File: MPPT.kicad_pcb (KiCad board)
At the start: 2 copper layers, 172.7 x 116.8 mm, 155 parts, among them J1 Solar Array, J2 Battery, J3 Car Power, J4 CAN_In, J5 CAN_Out, Q1 NMOS, Q2 NMOS, SW1 RESET, SW2 CAN Address, U1 PQMC3-D12-S9-S, U2 Nucleo_L432KC, U3 UCC37321, U4 INA210, U5 ADM3055E, U6 INA210, U7 CDSOT23-T24CAN

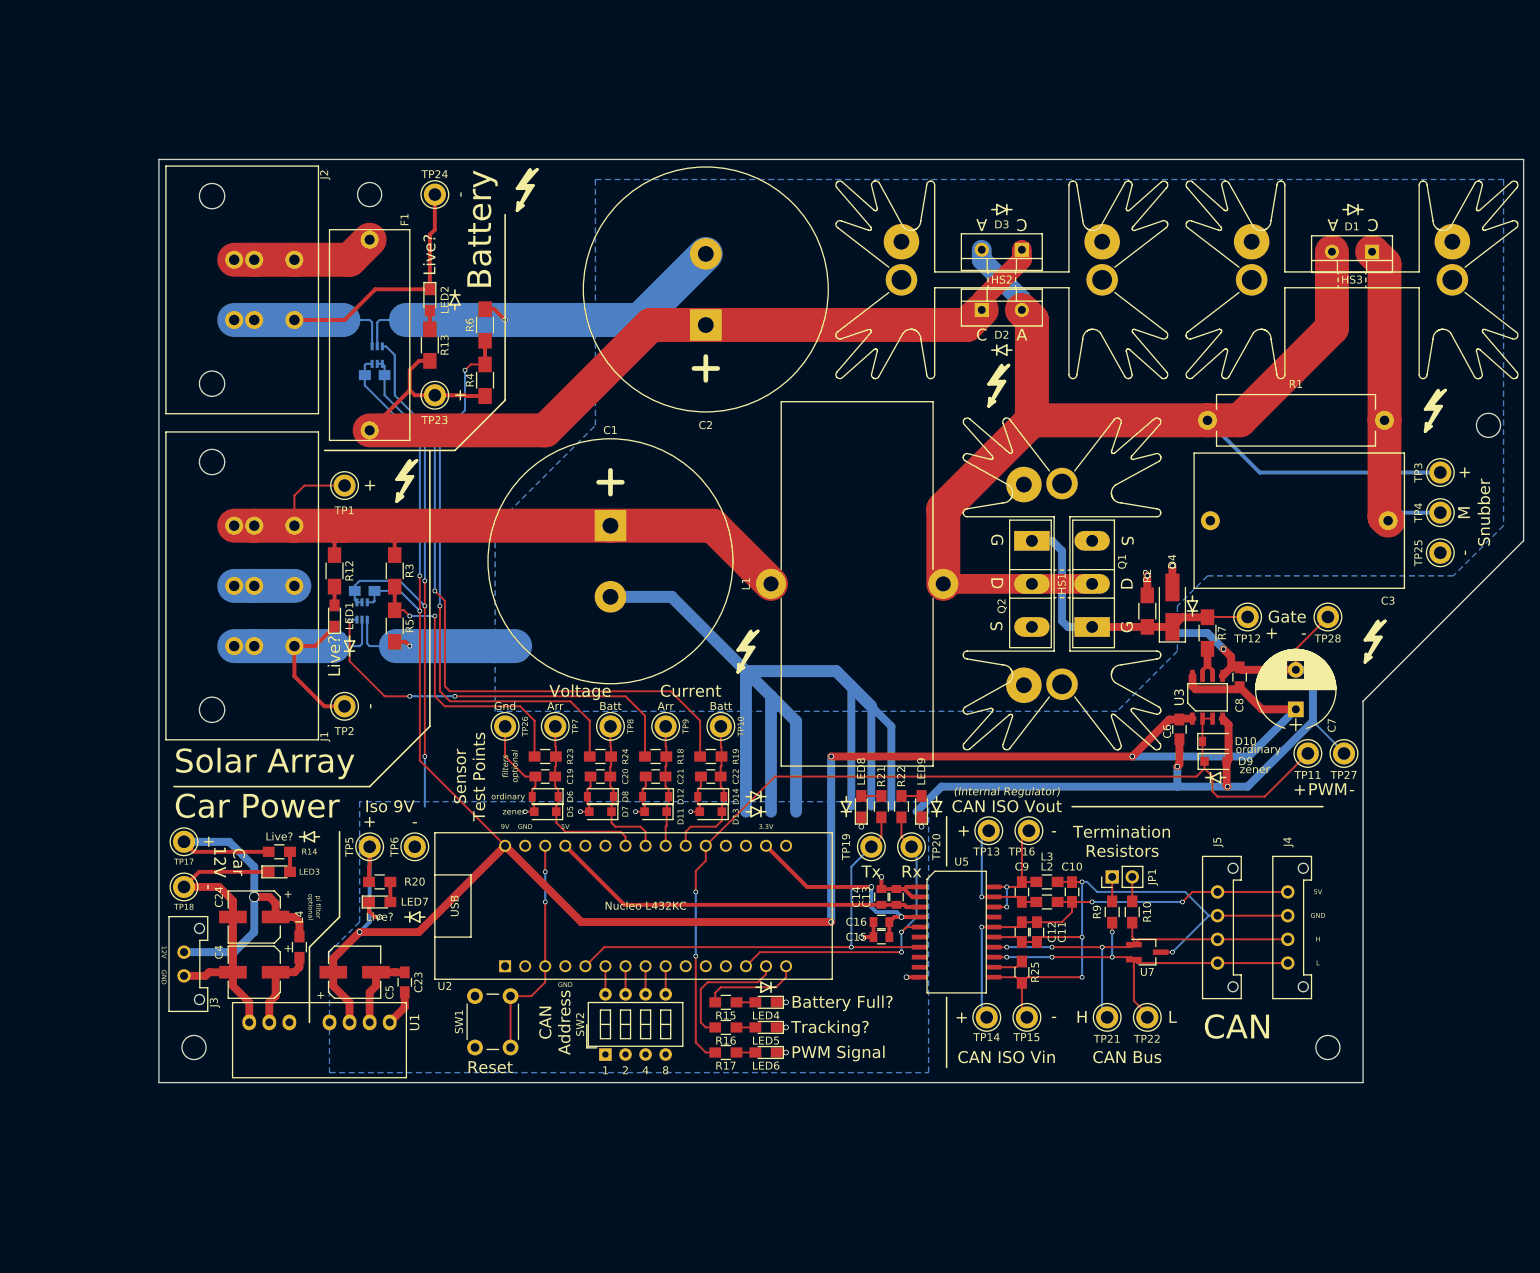
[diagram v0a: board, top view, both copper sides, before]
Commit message: Major MPPT Board overhaul. Schematic advanced to Rev 3.2. Layout advanced to Rev 1.3. README and documentation updated. Parts list synchronized, standardized, and referenced.
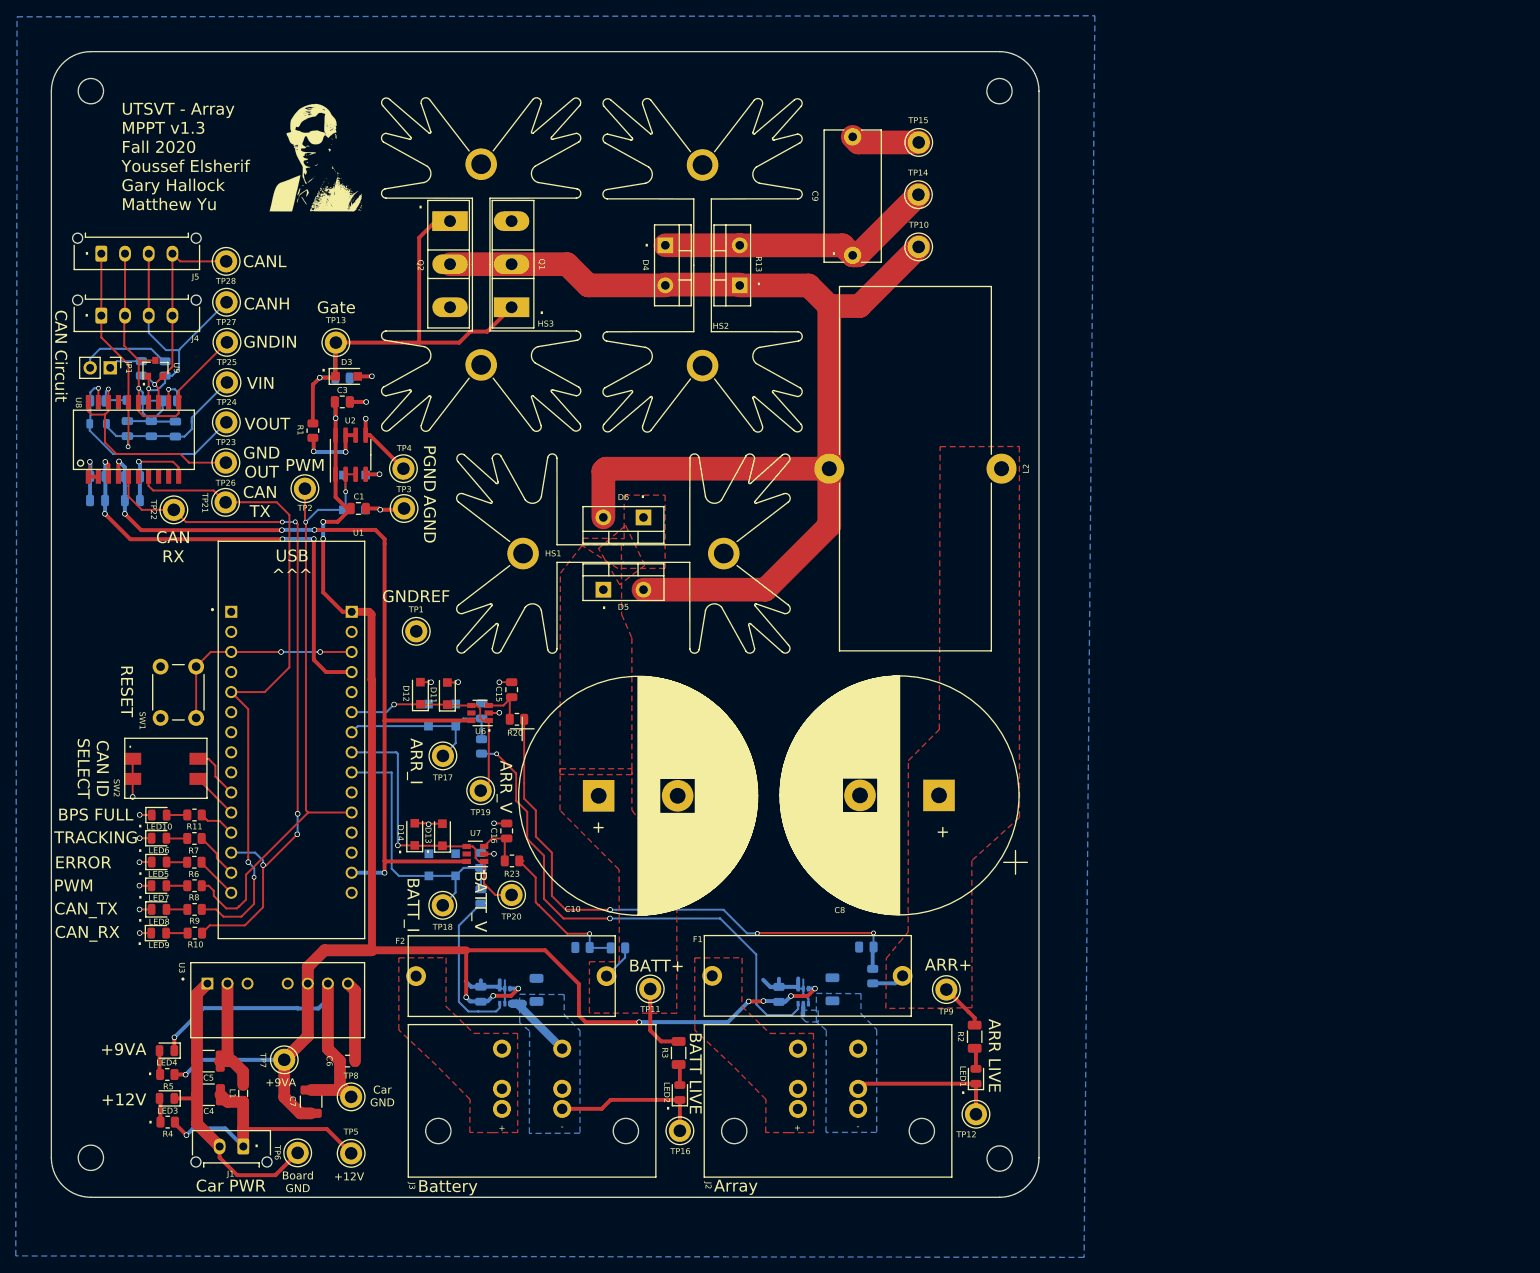
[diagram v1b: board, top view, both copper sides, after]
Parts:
- removed REF** (x6): Symbol_HighVoltage_Small, UTSVT_Special:Symbol_HighVoltage_Small
- removed REF** (x6): SolderWirePad_single_2mmDrill, Wire_Pads:SolderWirePad_single_2mmDrill
- removed REF** (x4): MountingHole_4-40_PanHead, UTSVT_Mechanical:MountingHole_4-40_PanHead
- removed REF** (x14): Diode_Symbol_Small, UTSVT_Special:Diode_Symbol_Small
- added F2: Fuse, MPPT-PrimaryPCB:05200101Z_Fuze_Holder_5x20_PCB_Mount, F.Cu at (62.7, 129.4)
- added G***: LOGO, UTSVT_Special:UTSVT_Logo_Symbol, B.Cu at (35.9, 27.7)
- added G***: LOGO, UTSVT_Special:Hallock_Image_Tiny, F.Cu at (50.5, 30.7)
- added H1: Top Left Mounting Hole, MountingHole:MountingHole_3.2mm_M3, F.Cu at (137.5, 157.5)
- added H2: Top Right Mounting Hole, MountingHole:MountingHole_3.2mm_M3, F.Cu at (22.5, 157.5)
- added H3: Bottom Left Mounting Hole, MountingHole:MountingHole_3.2mm_M3, F.Cu at (137.5, 22.5)
- added H4: Bottom Right Mounting Hole, MountingHole:MountingHole_3.2mm_M3, F.Cu at (22.5, 22.5)
- added LED10: BPS Full (Blue), LED_SMD:LED_0805_2012Metric, F.Cu at (31.1, 114.1)
- added R26: 60, Resistor_SMD:R_0805_2012Metric, B.Cu at (28.9, 57.6)
- added U8: ADM3055E, MPPT-PrimaryPCB:ADM3055EBRIZ, F.Cu at (27.9, 66.5)
- added U9: CDSOT23-T24CAN, Package_TO_SOT_SMD:SOT-23, F.Cu at (30.7, 57.5)
- C1: value 1000uF -> 0.1uF; footprint UTSVT_Passive:CP_Radial_D31mm_P9mm -> Capacitor_SMD:C_0805_2012Metric
- C10: value 0.22u -> 1000uF; footprint Capacitors_SMD:C_0805_HandSoldering -> Capacitor_THT:CP_Radial_D30.0mm_P10.00mm_SnapIn
- C11: value 0.1u -> 0.1uF; footprint Capacitors_SMD:C_0805_HandSoldering -> Capacitor_SMD:C_0805_2012Metric; moved to B.Cu
- C12: value 0.01u -> 1uF; footprint Capacitors_SMD:C_0805_HandSoldering -> Capacitor_SMD:C_0805_2012Metric; moved to B.Cu
- C13: value 10u -> 0.1uF; footprint Capacitors_SMD:C_0805 -> Capacitor_SMD:C_0805_2012Metric; moved to B.Cu
- C14: value 0.1u -> 1uF; footprint Capacitors_SMD:C_0805 -> Capacitor_SMD:C_0805_2012Metric; moved to B.Cu
- C15: value 0.1u -> 1uF; footprint Capacitors_SMD:C_0805 -> Capacitor_SMD:C_0805_2012Metric
- C16: value 0.01u -> 1uF; footprint Capacitors_SMD:C_0805 -> Capacitor_SMD:C_0805_2012Metric
- C17: value 0.1uF -> 10uF; footprint Capacitors_SMD:C_0805_HandSoldering -> Capacitor_SMD:C_0805_2012Metric
- C18: footprint Capacitors_SMD:C_0805_HandSoldering -> Capacitor_SMD:C_0805_2012Metric
- C19: value 1uF -> 0.1uF; footprint Capacitors_SMD:C_0805_HandSoldering -> Capacitor_SMD:C_0805_2012Metric; moved to B.Cu
- C2: value 1000uF -> 1uF; footprint UTSVT_Passive:CP_Radial_D31mm_P9mm -> Capacitor_SMD:C_0805_2012Metric; moved to B.Cu
- C20: value 1uF -> 0.01uF; footprint Capacitors_SMD:C_0805_HandSoldering -> Capacitor_SMD:C_0805_2012Metric; moved to B.Cu
- C21: value 1uF -> 0.22uF; footprint Capacitors_SMD:C_0805_HandSoldering -> Capacitor_SMD:C_0805_2012Metric; moved to B.Cu
- C22: value 1uF -> 10uF; footprint Capacitors_SMD:C_0805_HandSoldering -> Capacitor_SMD:C_0805_2012Metric; moved to B.Cu
- C23: value 10u -> 0.01uF; footprint Capacitors_SMD:C_0805_HandSoldering -> Capacitor_SMD:C_0805_2012Metric; moved to B.Cu
- C24: value 100u -> 0.1uF; footprint Capacitors_SMD:CP_Elec_6.3x7.7 -> Capacitor_SMD:C_0805_2012Metric; moved to B.Cu
- C3: value CP -> 0.1uF; footprint MPPT_Custom:C_Rect_L26.5mm_W17.0mm_P22.50mm_MKS4 -> Capacitor_SMD:C_0805_2012Metric
- C4: value 47u -> 100uF; footprint Capacitors_SMD:CP_Elec_6.3x5.3 -> Capacitor_SMD:C_1210_3225Metric
- C5: value 100u -> 47uF; footprint Capacitors_SMD:CP_Elec_6.3x7.7 -> Capacitor_SMD:C_1210_3225Metric
- C6: value 0.1u -> 10uF; footprint Capacitors_SMD:C_0805_HandSoldering -> Capacitor_SMD:C_0805_2012Metric
- C7: value 1u -> 100uF; footprint Capacitors_THT:CP_Radial_D10.0mm_P5.00mm -> Capacitor_SMD:C_1210_3225Metric
- C8: value 0.1u -> 1000uF; footprint Capacitors_SMD:C_0805_HandSoldering -> Capacitor_THT:CP_Radial_D30.0mm_P10.00mm_SnapIn
- C9: value 10u -> CP; footprint Capacitors_SMD:C_0805_HandSoldering -> Capacitor_THT:C_Rect_L16.5mm_W7.0mm_P15.00mm_MKT
- D1: value Schottky -> 3.9V Zener; footprint TO_SOT_Packages_THT:TO-220-2_Vertical -> Diode_SMD:D_SOD-123F; moved to B.Cu
- D10, D8: footprint Diodes_SMD:D_SOD-123 -> Diode_SMD:D_SOD-123F; moved to B.Cu
- D11, D13: value 4V Zener -> 3.9V Zener; footprint Diodes_SMD:D_SOD-123F -> Diode_SMD:D_SOD-123F
- D12, D14: footprint Diodes_SMD:D_SOD-123 -> Diode_SMD:D_SOD-123F
- D2: value Schottky -> Diode; footprint TO_SOT_Packages_THT:TO-220-2_Vertical -> Diode_SMD:D_SOD-123F; moved to B.Cu
- D3: value Schottky -> 16.3V Zener; footprint TO_SOT_Packages_THT:TO-220-2_Vertical -> Diode_SMD:D_SOD-123F
- D4: value 18V Zener -> Schottky; footprint Diodes_SMD:D_SMA_Handsoldering -> Package_TO_SOT_THT:TO-220-2_Vertical
- D5: value 4V Zener -> Schottky; footprint Diodes_SMD:D_SOD-123F -> Package_TO_SOT_THT:TO-220-2_Vertical
- D6: value Diode -> Schottky; footprint Diodes_SMD:D_SOD-123 -> Package_TO_SOT_THT:TO-220-2_Vertical
- D7, D9: value 4V Zener -> 3.9V Zener; footprint Diodes_SMD:D_SOD-123F -> Diode_SMD:D_SOD-123F; moved to B.Cu
- F1: footprint UTSVT_Passive:LittelFuse_OMNIBLOK_520Series_PCB -> MPPT-PrimaryPCB:05200101Z_Fuze_Holder_5x20_PCB_Mount
- HS1: value Heatsink_Fischer_SK129-STS_42x25mm_2xDrill2.5mm -> Schottky Diode Heatsink; footprint Heatsinks:Heatsink_Fischer_SK129-STS_42x25mm_2xDrill2.5mm -> Heatsink:Heatsink_Fischer_SK129-STS_42x25mm_2xDrill2.5mm
- HS2: value Heatsink_Fischer_SK129-STS_42x25mm_2xDrill2.5mm -> Snubber Heatsink; footprint Heatsinks:Heatsink_Fischer_SK129-STS_42x25mm_2xDrill2.5mm -> Heatsink:Heatsink_Fischer_SK129-STS_42x25mm_2xDrill2.5mm
- HS3: value Heatsink_Fischer_SK129-STS_42x25mm_2xDrill2.5mm -> MOSFET Heatsink; footprint Heatsinks:Heatsink_Fischer_SK129-STS_42x25mm_2xDrill2.5mm -> Heatsink:Heatsink_Fischer_SK129-STS_42x25mm_2xDrill2.5mm
- J1: value Solar Array -> Car Power; footprint UTSVT_Connectors:PhoenixContact_PowerCombicon5_GF_3x7.62mm -> Connector_Molex:Molex_Micro-Fit_3.0_43650-0215_1x02_P3.00mm_Vertical
- J2: value Battery -> Solar Array; footprint UTSVT_Connectors:PhoenixContact_PowerCombicon5_GF_2x7.62mm -> MPPT-PrimaryPCB:PhoenixContact_PowerCombicon5_GF_2x7.62mm
- J3: value Car Power -> Battery; footprint UTSVT_Connectors:Molex_MicroFit3.0_1x2xP3.00mm_PolarizingPeg_Vertical -> MPPT-PrimaryPCB:PhoenixContact_PowerCombicon5_GF_2x7.62mm
- J4, J5: footprint UTSVT_Connectors:Molex_MicroFit3.0_1x4xP3.00mm_PolarizingPeg_Vertical -> Connector_Molex:Molex_Micro-Fit_3.0_43650-0415_1x04_P3.00mm_Vertical
- JP1: footprint Pin_Headers:Pin_Header_Straight_1x02_Pitch2.54mm -> Connector_PinHeader_2.54mm:PinHeader_1x02_P2.54mm_Vertical
- L1: value 560uH -> 4.7uH; footprint Inductors_THT:L_Toroid_Vertical_L46.0mm_W19.1mm_P21.80mm_Bourns_5700 -> Inductor_SMD:L_0805_2012Metric
- L2: value 2k -> 560uH; footprint Inductors_SMD:L_0805_HandSoldering -> MPPT-PrimaryPCB:L_Toroid_Vertical_L46.0mm_W19.1mm_P21.80mm_Bourns_5700
- L3: value 2k -> 1.8kH; footprint Inductors_SMD:L_0805_HandSoldering -> Inductor_SMD:L_0805_2012Metric; moved to B.Cu
- L4: value 4.7u -> 1.8kH; footprint Inductors_SMD:L_0805_HandSoldering -> Inductor_SMD:L_0805_2012Metric; moved to B.Cu
- LED1: value Array Live? -> Array Live (Green); footprint LEDs:LED_0805_HandSoldering -> LED_SMD:LED_0805_2012Metric
- LED2: value Battery Live? -> Battery Live (Green); footprint LEDs:LED_0805_HandSoldering -> LED_SMD:LED_0805_2012Metric
- LED3: value Car Power Live? -> Car Power Live (Green); footprint LEDs:LED_0805_HandSoldering -> LED_SMD:LED_0805_2012Metric
- LED4: value Battery Full? -> Device 9V Live (Green); footprint LEDs:LED_0805_HandSoldering -> LED_SMD:LED_0805_2012Metric
- LED5: value Tracking? -> Error (Amber); footprint LEDs:LED_0805_HandSoldering -> LED_SMD:LED_0805_2012Metric
- LED6: value PWM -> Tracking (Blue); footprint LEDs:LED_0805_HandSoldering -> LED_SMD:LED_0805_2012Metric
- LED7: value Iso 9V Live? -> PWM (Blue); footprint LEDs:LED_0805_HandSoldering -> LED_SMD:LED_0805_2012Metric
- LED8: value CAN_Tx -> CAN_Tx (Blue); footprint LEDs:LED_0805_HandSoldering -> LED_SMD:LED_0805_2012Metric
- LED9: value CAN_Rx -> CAN_Rx (Blue); footprint LEDs:LED_0805_HandSoldering -> LED_SMD:LED_0805_2012Metric
- Q1, Q2: footprint TO_SOT_Packages_THT:TO-247_TO-3P_Vertical -> Package_TO_SOT_THT:TO-247-3_Vertical
- R1: value R -> 1.5; footprint Resistors_THT:R_Axial_Power_L20.0mm_W6.4mm_P22.40mm -> Resistor_SMD:R_0805_2012Metric
- R10, R9: value 60 -> 330; footprint Resistors_SMD:R_0805_HandSoldering -> Resistor_SMD:R_0805_2012Metric
- R11, R8: value 2m -> 330; footprint Resistors_SMD:R_2512_HandSoldering -> Resistor_SMD:R_0805_2012Metric; moved to F.Cu
- R12: value 40K -> 10k; footprint Resistors_SMD:R_1206_HandSoldering -> Resistor_SMD:R_0805_2012Metric; moved to B.Cu
- R13: value 40K -> R; footprint Resistors_SMD:R_1206_HandSoldering -> Package_TO_SOT_THT:TO-220-2_Vertical
- R14: value 2K -> 2m; footprint Resistors_SMD:R_0805_HandSoldering -> Resistor_SMD:R_1206_3216Metric; moved to B.Cu
- R15, R17: value 330R -> 1.7k; footprint Resistors_SMD:R_0805_HandSoldering -> Resistor_SMD:R_0805_2012Metric; moved to B.Cu
- R16: value 330R -> 2m; footprint Resistors_SMD:R_0805_HandSoldering -> Resistor_SMD:R_1206_3216Metric; moved to B.Cu
- R18: value 1.7k -> 100k; footprint Resistors_SMD:R_0805_HandSoldering -> Resistor_SMD:R_0805_2012Metric; moved to B.Cu
- R19: value 1.7k -> 2k; footprint Resistors_SMD:R_0805_HandSoldering -> Resistor_SMD:R_0805_2012Metric; moved to B.Cu
- R2: value 10k -> 15k; footprint Resistors_SMD:R_1206_HandSoldering -> Resistor_SMD:R_1206_3216Metric
- R20: value 1K -> 1.7k; footprint Resistors_SMD:R_0805_HandSoldering -> Resistor_SMD:R_0805_2012Metric
- R21: value 330R -> 100k; footprint Resistors_SMD:R_0805_HandSoldering -> Resistor_SMD:R_0805_2012Metric; moved to B.Cu
- R22: value 330R -> 2k; footprint Resistors_SMD:R_0805_HandSoldering -> Resistor_SMD:R_0805_2012Metric; moved to B.Cu
- R23: footprint Resistors_SMD:R_0805_HandSoldering -> Resistor_SMD:R_0805_2012Metric
- R24: value 1.7k -> 0; footprint Resistors_SMD:R_0805_HandSoldering -> Resistor_SMD:R_0805_2012Metric; moved to B.Cu
- R25: value 0 -> 60; footprint Resistors_SMD:R_0805_HandSoldering -> Resistor_SMD:R_0805_2012Metric; moved to B.Cu
- R3: value 100k -> 27k; footprint Resistors_SMD:R_1206_HandSoldering -> Resistor_SMD:R_1206_3216Metric
- R4: value 100k -> 1.5k; footprint Resistors_SMD:R_1206_HandSoldering -> Resistor_SMD:R_0805_2012Metric
- R5: value 2k -> 1.1k; footprint Resistors_SMD:R_1206_HandSoldering -> Resistor_SMD:R_0805_2012Metric
- R6: value 2k -> 330; footprint Resistors_SMD:R_1206_HandSoldering -> Resistor_SMD:R_0805_2012Metric
- R7: value 1R5 -> 330; footprint Resistors_SMD:R_1206_HandSoldering -> Resistor_SMD:R_0805_2012Metric
- SW1: footprint Buttons_Switches_THT:SW_PUSH_6mm -> Button_Switch_THT:SW_PUSH_6mm
- SW2: value CAN Address -> SW_DIP_x02; footprint Buttons_Switches_THT:SW_DIP_x4_W7.62mm_Slide_LowProfile -> MPPT-PrimaryPCB:ADF02ST04_DIP_Switch_2_POS
- TP1: value +ARR -> GND; footprint Measurement_Points:Test_Point_Keystone_5005-5009_Compact -> TestPoint:TestPoint_Keystone_5005-5009_Compact
- TP10: value Batt_I -> +SNUB; footprint Measurement_Points:Test_Point_Keystone_5005-5009_Compact -> TestPoint:TestPoint_Keystone_5005-5009_Compact
- TP11: value PWM -> +BATT; footprint Measurement_Points:Test_Point_Keystone_5005-5009_Compact -> TestPoint:TestPoint_Keystone_5005-5009_Compact
- TP12: value GATE -> -ARR; footprint Measurement_Points:Test_Point_Keystone_5005-5009_Compact -> TestPoint:TestPoint_Keystone_5005-5009_Compact
- TP13: value CAN_ISO_Vout -> GATE; footprint Measurement_Points:Test_Point_Keystone_5005-5009_Compact -> TestPoint:TestPoint_Keystone_5005-5009_Compact
- TP14: value CAN_ISO_Vin -> M_SNUB; footprint Measurement_Points:Test_Point_Keystone_5005-5009_Compact -> TestPoint:TestPoint_Keystone_5005-5009_Compact
- TP15: value CAN_ISO_GndIn -> -SNUB; footprint Measurement_Points:Test_Point_Keystone_5005-5009_Compact -> TestPoint:TestPoint_Keystone_5005-5009_Compact
- TP16: value CAN_ISO_GndOut -> -BATT; footprint Measurement_Points:Test_Point_Keystone_5005-5009_Compact -> TestPoint:TestPoint_Keystone_5005-5009_Compact
- TP17: value Car +12V -> Arr_I; footprint Measurement_Points:Test_Point_Keystone_5005-5009_Compact -> TestPoint:TestPoint_Keystone_5005-5009_Compact
- TP18: value Car GND -> Batt_I; footprint Measurement_Points:Test_Point_Keystone_5005-5009_Compact -> TestPoint:TestPoint_Keystone_5005-5009_Compact
- TP19: value CAN_Tx -> Arr_V; footprint Measurement_Points:Test_Point_Keystone_5005-5009_Compact -> TestPoint:TestPoint_Keystone_5005-5009_Compact
- TP2: value -ARR -> PWM; footprint Measurement_Points:Test_Point_Keystone_5005-5009_Compact -> TestPoint:TestPoint_Keystone_5005-5009_Compact
- TP20: value CAN_Rx -> Batt_V; footprint Measurement_Points:Test_Point_Keystone_5005-5009_Compact -> TestPoint:TestPoint_Keystone_5005-5009_Compact
- TP21: value CAN_H -> CAN_Tx; footprint Measurement_Points:Test_Point_Keystone_5005-5009_Compact -> TestPoint:TestPoint_Keystone_5005-5009_Compact
- TP22: value CAN_L -> CAN_Rx; footprint Measurement_Points:Test_Point_Keystone_5005-5009_Compact -> TestPoint:TestPoint_Keystone_5005-5009_Compact
- TP23: value +BATT -> CAN_ISO_Vout; footprint Measurement_Points:Test_Point_Keystone_5005-5009_Compact -> TestPoint:TestPoint_Keystone_5005-5009_Compact
- TP24: value -BATT -> CAN_ISO_Vin; footprint Measurement_Points:Test_Point_Keystone_5005-5009_Compact -> TestPoint:TestPoint_Keystone_5005-5009_Compact
- TP25: value -SNUB -> CAN_ISO_GndIn; footprint Measurement_Points:Test_Point_Keystone_5005-5009_Compact -> TestPoint:TestPoint_Keystone_5005-5009_Compact
- TP26: value GND -> CAN_ISO_GndOut; footprint Measurement_Points:Test_Point_Keystone_5005-5009_Compact -> TestPoint:TestPoint_Keystone_5005-5009_Compact
- TP27: value AGND -> CAN_H; footprint Measurement_Points:Test_Point_Keystone_5005-5009_Compact -> TestPoint:TestPoint_Keystone_5005-5009_Compact
- TP28: value PGND -> CAN_L; footprint Measurement_Points:Test_Point_Keystone_5005-5009_Compact -> TestPoint:TestPoint_Keystone_5005-5009_Compact
- TP3: value +SNUB -> AGND; footprint Measurement_Points:Test_Point_Keystone_5005-5009_Compact -> TestPoint:TestPoint_Keystone_5005-5009_Compact
- TP4: value M_SNUB -> PGND; footprint Measurement_Points:Test_Point_Keystone_5005-5009_Compact -> TestPoint:TestPoint_Keystone_5005-5009_Compact
- TP5: value +9VA -> Car +12V; footprint Measurement_Points:Test_Point_Keystone_5005-5009_Compact -> TestPoint:TestPoint_Keystone_5005-5009_Compact
- TP6: value GNDP -> Car GND; footprint Measurement_Points:Test_Point_Keystone_5005-5009_Compact -> TestPoint:TestPoint_Keystone_5005-5009_Compact
- TP7: value Arr_V -> +9VA; footprint Measurement_Points:Test_Point_Keystone_5005-5009_Compact -> TestPoint:TestPoint_Keystone_5005-5009_Compact
- TP8: value Batt_V -> Device GND; footprint Measurement_Points:Test_Point_Keystone_5005-5009_Compact -> TestPoint:TestPoint_Keystone_5005-5009_Compact
- TP9: value Arr_I -> +ARR; footprint Measurement_Points:Test_Point_Keystone_5005-5009_Compact -> TestPoint:TestPoint_Keystone_5005-5009_Compact
- U1: value PQMC3-D12-S9-S -> Nucleo_L432KC; footprint UTSVT_ICs:CUI_PQMC3-S -> MPPT-PrimaryPCB:MODULE_NUCLEO-L432KC
- U2: value Nucleo_L432KC -> UCC37321; footprint UTSVT_Special:NucleoL432KC -> Package_SO:SOIC-8_3.9x4.9mm_P1.27mm
- U3: value UCC37321 -> PQMC3-D12-S9-S; footprint UTSVT_ICs:SOIC-8_4.00x5.00mm_Pitch1.27mm -> MPPT-PrimaryPCB:490_PQMC3_D12_S12_S
- U4: footprint UTSVT_ICs:SOIC-6_1.40x2.15mm_Pitch0.65mm -> MPPT-PrimaryPCB:SC70-6
- U5: value ADM3055E -> INA210; footprint UTSVT_ICs:SOIC-20W_7.5x15.4mm_Pitch1.27mm -> MPPT-PrimaryPCB:SC70-6; moved to B.Cu
- U6: value INA210 -> MAX40075AUT+; footprint UTSVT_ICs:SOIC-6_1.40x2.15mm_Pitch0.65mm -> Package_TO_SOT_SMD:SOT-23-6; moved to F.Cu
- U7: value CDSOT23-T24CAN -> MAX40075AUT+; footprint TO_SOT_Packages_SMD:SOT-23W_Handsoldering -> Package_TO_SOT_SMD:SOT-23-6
- moved J4 166.9 mm to (23.8, 50.9), turned to 0 degrees
- moved J5 162.7 mm to (23.8, 43.0), turned to 0 degrees
- moved TP25 155.9 mm to (39.7, 54.3)
- moved TP27 152.5 mm to (39.7, 49.2), turned to 90 degrees
- moved TP28 146.5 mm to (39.6, 44.0), turned to 90 degrees
- moved JP1 142.2 mm to (24.9, 57.5), turned to 270 degrees
- moved TP22 138.9 mm to (33.0, 75.5), turned to 0 degrees
- moved C7 134.2 mm to (50.4, 150.4)
- moved L3 133.4 mm to (23.4, 64.6)
- moved C3 133.2 mm to (54.3, 61.8), turned to 0 degrees
- moved D1 132.9 mm to (55.9, 75.5), turned to 0 degrees
- moved R25 132.7 mm to (31.9, 57.6)
- moved TP4 131.4 mm to (62.1, 70.3), turned to 270 degrees
- moved TP3 131.2 mm to (62.1, 75.3), turned to 270 degrees
- moved R7 130.8 mm to (35.6, 117.1), turned to 0 degrees
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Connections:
- C1 pad 1: /+Arr -> GNDREF
- C1 pad 2: GNDPWR -> +9VA
- C10 pad 1: Net-(C10-Pad1) -> /+Batt
- C10 pad 2: Net-(C10-Pad2) -> GNDREF
- C11 pad 1: Net-(C10-Pad1) -> +9VA
- C11 pad 2: Net-(C10-Pad2) -> GNDREF
- C12 pad 1: Net-(C10-Pad1) -> /Array_Current
- C12 pad 2: Net-(C10-Pad2) -> GNDREF
- C13 pad 1: +5V -> +9VA
- C13 pad 2: GNDPWR -> GNDREF
- C14 pad 1: +5V -> /Battery_Current
- C14 pad 2: GNDPWR -> GNDREF
- C15 pad 1: +3V3 -> Net-(C15-Pad1)
- C15 pad 2: GNDPWR -> GNDREF
- C16 pad 1: +3V3 -> Net-(C16-Pad1)
- C16 pad 2: GNDPWR -> GNDREF
- C17 pad 1: +9VA -> +5V
- C17 pad 2: GNDPWR -> GNDREF
- C18 pad 1: +9VA -> +5V
- C18 pad 2: GNDPWR -> GNDREF
- C19 pad 1: /Array_Voltage -> +3V3
- C19 pad 2: GNDPWR -> GNDREF
- C2 pad 1: /+Batt -> +9VA
- C2 pad 2: GNDPWR -> GNDREF
- C20 pad 1: /Battery_Voltage -> +3V3
- C20 pad 2: GNDPWR -> GNDREF
- C21 pad 1: /Array_Current -> Net-(C21-Pad1)
- C21 pad 2: GNDPWR -> Net-(C21-Pad2)
- C22 pad 1: /Battery_Current -> Net-(C22-Pad1)
- C22 pad 2: GNDPWR -> Net-(C22-Pad2)
- C23 pad 1: GNDPWR -> Net-(C22-Pad1)
- C23 pad 2: Net-(C23-Pad2) -> Net-(C22-Pad2)
- C24 pad 1: +12V -> Net-(C22-Pad1)
- C24 pad 2: GNDREF -> Net-(C22-Pad2)
- C3 pad 1: Net-(C3-Pad1) -> +9VA
- C3 pad 2: GNDPWR -> GNDREF
- C4 pad 1: Net-(C4-Pad1) -> +12V
- C4 pad 2: GNDREF -> GNDPWR
- C5 pad 1: +9VA -> Net-(C5-Pad1)
- C6 pad 1: GNDPWR -> GNDREF
- C6 pad 2: +9VA -> Net-(C6-Pad2)
- C7 pad 2: GNDPWR -> GNDREF
- C8 pad 1: +9VA -> /+Arr
- C8 pad 2: GNDPWR -> GNDREF
- C9 pad 2: Net-(C9-Pad2) -> GNDREF
- D1 pad 1: Net-(C3-Pad1) -> /PWM
- D1 pad 2: Net-(D1-Pad2) -> GNDREF
- D10 pad 1: /PWM -> /Battery_Current
- D10 pad 2: GNDPWR -> GNDREF
- D11 pad 1: /Array_Current -> /Array_Voltage
- D11 pad 2: GNDPWR -> GNDREF
- D12 pad 1: /Array_Current -> /Array_Voltage
- D12 pad 2: GNDPWR -> GNDREF
- D13 pad 1: /Battery_Current -> /Battery_Voltage
- D13 pad 2: GNDPWR -> GNDREF
- D14 pad 1: /Battery_Current -> /Battery_Voltage
- D14 pad 2: GNDPWR -> GNDREF
- D2 pad 1: /+Batt -> /PWM
- D2 pad 2: Net-(D1-Pad2) -> GNDREF
- D3 pad 1: /+Batt -> /Drive_PWM
- D3 pad 2: Net-(D1-Pad2) -> GNDREF
- D4 pad 1: /Drive_PWM -> Net-(C9-Pad1)
- D4 pad 2: GNDPWR -> Net-(D4-Pad2)
- D5 pad 1: /Array_Voltage -> /+Batt
- D5 pad 2: GNDPWR -> Net-(D4-Pad2)
- D6 pad 1: /Array_Voltage -> /+Batt
- D6 pad 2: GNDPWR -> Net-(D4-Pad2)
- D7 pad 1: /Battery_Voltage -> /Array_Current
- D7 pad 2: GNDPWR -> GNDREF
- D8 pad 1: /Battery_Voltage -> /Array_Current
- D8 pad 2: GNDPWR -> GNDREF
- D9 pad 1: /PWM -> /Battery_Current
- D9 pad 2: GNDPWR -> GNDREF
- F1 pad 2: /+Batt -> /+Arr
- J1 pad 1: /+Arr -> +12V
- J1 pad 2: Net-(J1-Pad2) -> GNDPWR
- J2 pad 2: /-Batt -> /-Arr
- J3 pad 1: +12V -> Net-(F2-Pad1)
- J3 pad 2: GNDREF -> /-Batt
- J4 pad 1: Net-(C10-Pad1) -> Net-(C22-Pad1)
- J4 pad 2: Net-(C10-Pad2) -> Net-(C22-Pad2)
- J5 pad 1: Net-(C10-Pad1) -> Net-(C22-Pad1)
- J5 pad 2: Net-(C10-Pad2) -> Net-(C22-Pad2)
- L1 pad 1: /+Arr -> +12V
- L1 pad 2: Net-(D1-Pad2) -> Net-(C5-Pad1)
- L2 pad 1: Net-(C10-Pad1) -> /+Arr
- L2 pad 2: Net-(C9-Pad1) -> Net-(D4-Pad2)
- L3 pad 1: Net-(C10-Pad2) -> Net-(C22-Pad1)
- L3 pad 2: Net-(C9-Pad2) -> Net-(C21-Pad1)
- L4 pad 1: +12V -> Net-(C22-Pad2)
- L4 pad 2: Net-(C4-Pad1) -> Net-(C21-Pad2)
- LED3 pad 1: GNDREF -> GNDPWR
- LED4 pad 1: GNDPWR -> GNDREF
- LED5 pad 1: GNDPWR -> GNDREF
- LED6 pad 1: GNDPWR -> GNDREF
- LED7 pad 1: GNDPWR -> GNDREF
- LED8 pad 1: GNDPWR -> GNDREF
- LED9 pad 1: GNDPWR -> GNDREF
- Q1 pad 2: Net-(D1-Pad2) -> Net-(D4-Pad2)
- Q1 pad 3: GNDPWR -> GNDREF
- Q2 pad 2: Net-(D1-Pad2) -> Net-(D4-Pad2)
- Q2 pad 3: GNDPWR -> GNDREF
- R1 pad 1: Net-(D1-Pad2) -> /Drive_PWM
- R1 pad 2: Net-(C3-Pad1) -> Net-(R1-Pad2)
- R10 pad 1: Net-(JP1-Pad2) -> Net-(LED9-Pad2)
- R10 pad 2: Net-(J4-Pad3) -> /CAN_Rx
- R11 pad 1: /-Batt -> Net-(LED10-Pad2)
- R11 pad 2: GNDPWR -> /BPS_Full
- R12 pad 1: Net-(LED1-Pad2) -> /Drive_PWM
- R12 pad 2: /+Arr -> GNDREF
- R13 pad 1: Net-(LED2-Pad2) -> Net-(D4-Pad2)
- R13 pad 2: /+Batt -> Net-(C9-Pad1)
- R14 pad 1: Net-(LED3-Pad2) -> GNDREF
- R14 pad 2: +12V -> /-Arr
- R15 pad 1: Net-(LED4-Pad2) -> Net-(R15-Pad1)
- R15 pad 2: /Battery_Full -> /Array_Current
- R16 pad 1: Net-(LED5-Pad2) -> /-Batt
- R16 pad 2: /Tracking -> GNDREF
- R17 pad 1: Net-(LED6-Pad2) -> Net-(R17-Pad1)
- R17 pad 2: /PWM -> /Battery_Current
- R18 pad 1: Net-(R18-Pad1) -> /+Arr
- R18 pad 2: /Array_Current -> Net-(R18-Pad2)
- R19 pad 1: Net-(R19-Pad1) -> Net-(R18-Pad2)
- R19 pad 2: /Battery_Current -> GNDREF
- R2 pad 1: /Drive_PWM -> Net-(LED1-Pad2)
- R2 pad 2: GNDPWR -> /+Arr
- R20 pad 1: Net-(LED7-Pad2) -> Net-(R18-Pad2)
- R20 pad 2: +9VA -> Net-(C15-Pad1)
- R21 pad 1: Net-(LED8-Pad2) -> /+Batt
- R21 pad 2: /CAN_Tx -> Net-(R21-Pad2)
- R22 pad 1: Net-(LED9-Pad2) -> Net-(R21-Pad2)
- R22 pad 2: /CAN_Rx -> GNDREF
- R23 pad 1: Net-(R23-Pad1) -> Net-(R21-Pad2)
- R23 pad 2: /Array_Voltage -> Net-(C16-Pad1)
- R24 pad 2: /Battery_Voltage -> Net-(C22-Pad2)
- R25 pad 1: Net-(R25-Pad1) -> Net-(JP1-Pad2)
- R25 pad 2: Net-(C10-Pad2) -> Net-(J4-Pad3)
- R3 pad 1: /+Arr -> Net-(LED2-Pad2)
- R3 pad 2: Net-(R23-Pad1) -> /+Batt
- R4 pad 1: /+Batt -> Net-(LED3-Pad2)
- R4 pad 2: Net-(R24-Pad1) -> +12V
- R5 pad 1: Net-(R23-Pad1) -> Net-(LED4-Pad2)
- R5 pad 2: GNDPWR -> +9VA
- R6 pad 1: Net-(R24-Pad1) -> Net-(LED5-Pad2)
- R6 pad 2: GNDPWR -> /Error
- R7 pad 1: /Drive_PWM -> Net-(LED6-Pad2)
- R7 pad 2: Net-(R7-Pad2) -> /Tracking
- R8 pad 1: GNDPWR -> Net-(LED7-Pad2)
- R8 pad 2: /-Arr -> /PWM
- R9 pad 1: Net-(JP1-Pad1) -> Net-(LED8-Pad2)
- R9 pad 2: Net-(J4-Pad4) -> /CAN_Tx
- SW1 pad 1: GNDPWR -> /Reset
- SW1 pad 2: /Reset -> GNDREF
- SW2 pad 1: GNDPWR -> GNDREF
- SW2 pad 2: GNDPWR -> GNDREF
- SW2 pad 3: GNDPWR -> Net-(SW2-Pad3)
- SW2 pad 4: GNDPWR -> Net-(SW2-Pad4)
- TP1 pad 1: /+Arr -> GNDREF
- TP10 pad 1: /Battery_Current -> Net-(D4-Pad2)
- TP11 pad 1: /PWM -> /+Batt
- TP12 pad 1: /Drive_PWM -> /-Arr
- TP13 pad 1: Net-(C9-Pad1) -> /Drive_PWM
- TP14 pad 1: Net-(C10-Pad1) -> Net-(C9-Pad1)
- TP15 pad 1: Net-(C10-Pad2) -> GNDREF
- TP16 pad 1: Net-(C9-Pad2) -> /-Batt
- TP17 pad 1: +12V -> /Array_Current
- TP18 pad 1: GNDREF -> /Battery_Current
- TP19 pad 1: /CAN_Tx -> /Array_Voltage
- TP2 pad 1: /-Arr -> /PWM
- TP20 pad 1: /CAN_Rx -> /Battery_Voltage
- TP21 pad 1: Net-(J4-Pad3) -> /CAN_Tx
- TP22 pad 1: Net-(J4-Pad4) -> /CAN_Rx
- TP23 pad 1: /+Batt -> Net-(C21-Pad1)
- TP24 pad 1: /-Batt -> Net-(C22-Pad1)
- TP25 pad 1: GNDPWR -> Net-(C22-Pad2)
- TP26 pad 1: GNDPWR -> Net-(C21-Pad2)
- TP27 pad 1: GNDPWR -> Net-(J4-Pad3)
- TP28 pad 1: GNDPWR -> Net-(J4-Pad4)
- TP3 pad 1: Net-(D1-Pad2) -> GNDREF
- TP4 pad 1: Net-(C3-Pad1) -> GNDREF
- TP5 pad 1: +9VA -> +12V
- TP7 pad 1: /Array_Voltage -> +9VA
- TP8 pad 1: /Battery_Voltage -> GNDREF
- TP9 pad 1: /Array_Current -> /+Arr
- U1 pad 1: GNDREF -> Net-(U1-Pad1)
- U1 pad 2: Net-(C4-Pad1) -> Net-(U1-Pad2)
- U1 pad 3: Net-(U1-Pad3) -> /Reset
- U1 pad 5: Net-(U1-Pad5) -> /CAN_Tx
- U1 pad 6: +9VA -> Net-(U1-Pad6)
- U1 pad 7: GNDPWR -> Net-(U1-Pad7)
- U1 pad 8: Net-(C23-Pad2) -> Net-(U1-Pad8)
- U2 pad 1: Net-(U2-Pad1) -> +9VA
- U2 pad 2: Net-(U2-Pad2) -> /PWM
- U2 pad 3: /Reset -> /PWM
- U2 pad 4: GNDPWR -> GNDREF
- U2 pad 5: /CAN_Tx -> GNDREF
- U2 pad 6: Net-(SW2-Pad8) -> Net-(R1-Pad2)
- U2 pad 7: Net-(SW2-Pad7) -> Net-(R1-Pad2)
- U2 pad 8: Net-(SW2-Pad6) -> +9VA
- U3 pad 1: +9VA -> GNDPWR
- U3 pad 2: /PWM -> Net-(C5-Pad1)
- U3 pad 3: /PWM -> Net-(U3-Pad3)
- U3 pad 5: GNDPWR -> Net-(U3-Pad5)
- U3 pad 6: Net-(R7-Pad2) -> +9VA
- U3 pad 7: Net-(R7-Pad2) -> GNDREF
- U3 pad 8: +9VA -> Net-(C6-Pad2)
- U4 pad 1: GNDPWR -> GNDREF
- U4 pad 2: GNDPWR -> GNDREF
- U4 pad 4: GNDPWR -> GNDREF
- U4 pad 6: Net-(R18-Pad1) -> Net-(R15-Pad1)
- U5 pad 1: GNDPWR -> GNDREF
- U5 pad 2: GNDPWR -> GNDREF
- U5 pad 3: +5V -> +9VA
- U5 pad 4: +3V3 -> /-Batt
- U5 pad 5: /CAN_Rx -> GNDREF
- U5 pad 6: Net-(U5-Pad6) -> Net-(R17-Pad1)
- U6 pad 1: GNDPWR -> /Array_Voltage
- U6 pad 2: GNDPWR -> GNDREF
- U6 pad 3: +9VA -> Net-(C15-Pad1)
- U6 pad 4: /-Batt -> /Array_Voltage
- U6 pad 5: GNDPWR -> Net-(U6-Pad5)
- U6 pad 6: Net-(R19-Pad1) -> +3V3
- U7 pad 1: Net-(J4-Pad3) -> /Battery_Voltage
- U7 pad 2: Net-(J4-Pad4) -> GNDREF
- U7 pad 3: Net-(C10-Pad2) -> Net-(C16-Pad1)
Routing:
- net GNDPWR: track 463.5 -> 38.8 mm, vias 23 -> 0
- net Net-(D4-Pad2): track 0.00 -> 153.9 mm
- net Net-(D1-Pad2): track 153.1 -> 0.00 mm
- net /+Batt: track 116.1 -> 14.0 mm
- net GNDREF: track 41.1 -> 142.6 mm, vias 0 -> 22
- net Net-(R19-Pad1): track 85.2 -> 0.00 mm, vias 1 -> 0
- net +3V3: track 28.4 -> 111.1 mm, vias 2 -> 5
- net Net-(C10-Pad2): track 79.1 -> 0.00 mm, vias 4 -> 0
- net /+Arr: track 89.1 -> 10.2 mm
- net +9VA: track 283.6 -> 204.9 mm, vias 6 -> 12
- net Net-(R18-Pad2): track 0.00 -> 71.2 mm, vias 0 -> 3
- net Net-(R24-Pad1): track 72.8 -> 4.64 mm, vias 2 -> 1
- net Net-(R15-Pad1): track 0.00 -> 65.7 mm, vias 0 -> 2
- net Net-(C22-Pad2): track 0.00 -> 58.9 mm, vias 0 -> 1
- net Net-(C10-Pad1): track 54.9 -> 0.00 mm, vias 3 -> 0
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- added copper zone on F.Cu, net /+Arr
- added copper zone on F.Cu, net /+Batt
- added copper zone on B.Cu, net /-Arr
- added copper zone on B.Cu, net /-Batt
- added copper zone on B.Cu, net GNDREF
- added copper zone on F.Cu, net Net-(F1-Pad1)
- added copper zone on F.Cu, net Net-(F2-Pad1)
- removed copper zone on B.Cu, net GNDPWR
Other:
- board size 172.7 x 116.8 mm -> 125 x 145 mm
- board text added: "+12V"
- board text added: "+9VA"
- board text added: "."
- board text added: "AGND"
- board text added: "ARR LIVE"
- board text added: "ARR+"
- board text added: "ARR_I"
- board text added: "ARR_V"
- board text added: "Array"
- board text added: "BATT LIVE"
- board text added: "BATT+"
- board text added: "BATT_I"
- board text added: "BATT_V"
- board text added: "BPS FULL"
- board text added: "Board GND"
- board text added: "CAN Circuit"
- board text added: "CAN ID SELECT"
- board text added: "CAN RX"
- board text added: "CAN TX"
- board text added: "CANH"
- board text added: "CANL"
- board text added: "CAN_RX"
- board text added: "CAN_TX"
- board text added: "Car GND"
- board text added: "Car PWR"
- board text added: "ERROR"
- board text added: "GND OUT"
- board text added: "GNDIN"
- board text added: "GNDREF"
- board text added: "I could've just used B.Cu for CAN_TX and CAN_RX since GNDPWR isn't in the way, but I was unsure how much crosstalk the digital signal might get."
- board text added: "In principle, I am concerned about routing thin analog signals across two power planes for high power systems. Especially in the case where the system is attempting to rapidly shift the voltage to maximize the current, sometimes in large steps, which may cause outsized current fluctuations and electromagnetic interference."
- board text added: "PGND"
- board text added: "RESET"
- board text added: "Star ground separating digital logic from analog."
- board text added: "TRACKING"
- board text added: "U4"
- board text added: "U5"
- board text added: "USB ^^^"
- board text added: "UTSVT - Array MPPT v1.3 Fall 2020 Youssef Elsherif Gary Hallock Matthew Yu"
- board text added: "Unused"
- board text added: "VIN"
- board text added: "VOUT"
- board text removed: "(Internal Regulator)"
- board text removed: "1"
- board text removed: "12V"
- board text removed: "2"
- board text removed: "3.3V"
- board text removed: "4"
- board text removed: "5V"
- board text removed: "8"
- board text removed: "9V"
- board text removed: "A"
- board text removed: "Arr"
- board text removed: "Batt"
- board text removed: "Battery Full?"
- board text removed: "C"
- board text removed: "CAN"
- board text removed: "CAN Address"
- board text removed: "CAN Bus"
- board text removed: "CAN ISO Vin"
- board text removed: "CAN ISO Vout"
- board text removed: "Car 12V"
- board text removed: "Car Power"
- board text removed: "Current"
- board text removed: "D"
- board text removed: "G"
- board text removed: "GND"
- board text removed: "Gnd"
- board text removed: "H"
- board text removed: "Iso 9V"
- board text removed: "L"
- board text removed: "Live?"
- board text removed: "M"
- board text removed: "NC"
- board text removed: "Optional: Ground Heat Sink be careful about isolation!"
- board text removed: "PWM Signal"
- board text removed: "Reset"
- board text removed: "Rx"
- board text removed: "S"
- board text removed: "Sensor Test Points"
- board text removed: "Snubber"
- board text removed: "Solar Array"
- board text removed: "Termination Resistors"
- board text removed: "Tracking?"
- board text removed: "Tx"
- board text removed: "Voltage"
- board text removed: "filters optional"
- board text removed: "ordinary"
- board text removed: "pi filter optional"
- board text removed: "zener"

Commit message: Addressed review.
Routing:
- net GNDREF: track 142.6 -> 149.6 mm, vias 22 -> 24
